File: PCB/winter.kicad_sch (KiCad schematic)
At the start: 131 parts, among them SW1 SW_Push, SW10 SW_Push, SW11 SW_Push, SW12 SW_Push, SW13 SW_Push, SW14 SW_Push, SW15 SW_Push, SW16 SW_Push, SW17 SW_Push, SW18 SW_Push, SW19 SW_Push, SW2 SW_Push, SW20 SW_Push, SW21 SW_Push, SW22 SW_Push, SW23 SW_Push, SW24 SW_Push, SW25 SW_Push, SW26 SW_Push, SW27 SW_Push, SW28 SW_Push, SW29 SW_Push, SW3 SW_Push, SW30 SW_Push, SW31 SW_Push, SW32 SW_Push, SW33 SW_Push, SW34 SW_Push, SW35 SW_Push, SW36 SW_Push, SW37 SW_Push, SW38 SW_Push, SW39 SW_Push, SW4 SW_Push, SW40 SW_Push, SW41 SW_Push, SW42 SW_Push, SW43 SW_Push, SW44 SW_Push, SW45 SW_Push, SW46 SW_Push, SW47 SW_Push, SW48 SW_Push, SW49 SW_Push, SW5 SW_Push, SW50 SW_Push, SW51 SW_Push, SW52 SW_Push, SW53 SW_Push, SW54 SW_Push, SW55 SW_Push, SW56 SW_Push, SW57 SW_Push, SW58 SW_Push, SW59 SW_Push, SW6 SW_Push, SW60 SW_Push, SW61 SW_Push, SW62 SW_Push, SW63 SW_Push, SW64 SW_Push, SW65 SW_Push, SW7 SW_Push, SW8 SW_Push, SW9 SW_Push, U1 RP2040-ZERO

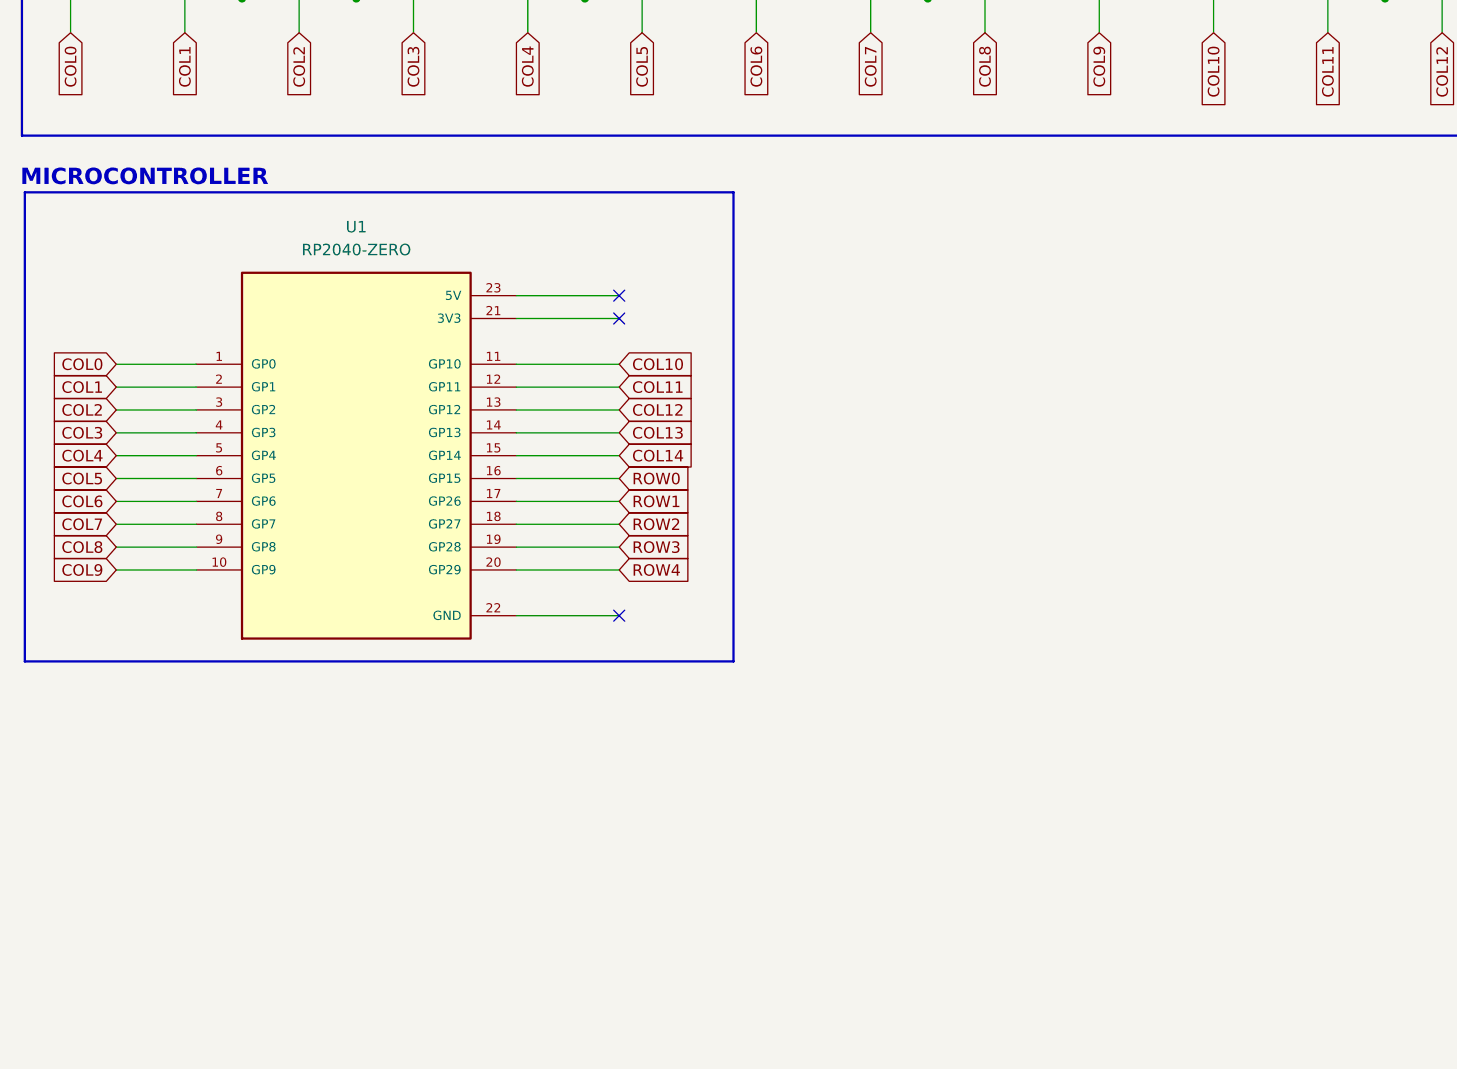
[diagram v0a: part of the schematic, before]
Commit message: changed mcu and added screen and knob
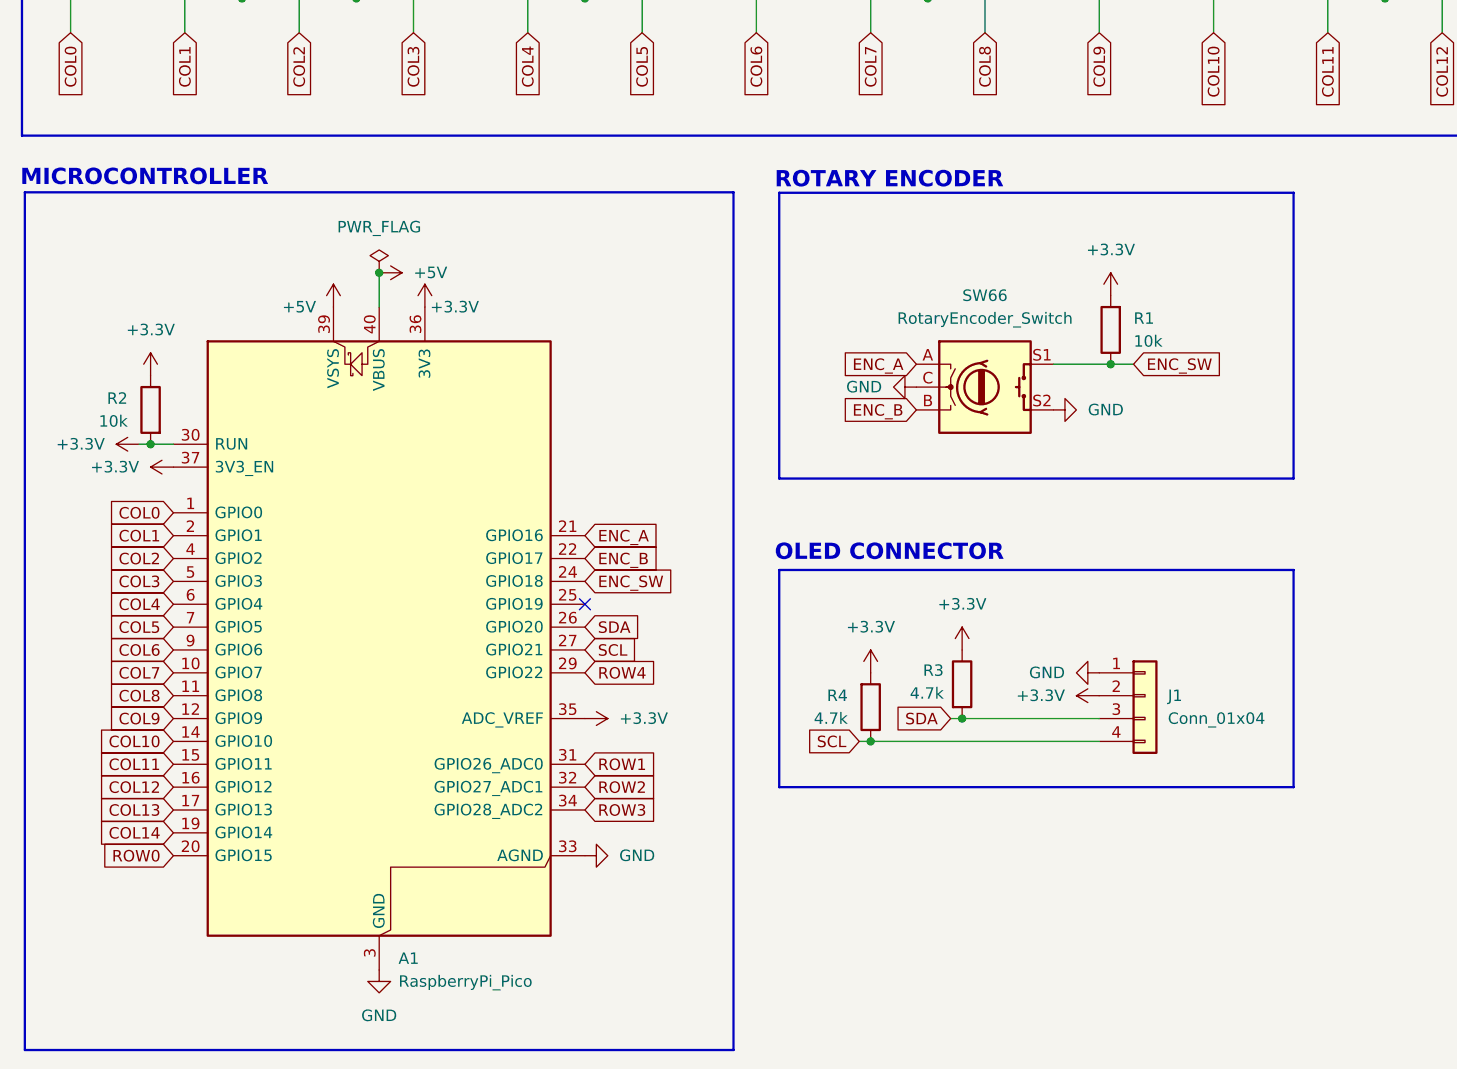
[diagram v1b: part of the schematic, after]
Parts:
- removed U1: RP2040-ZERO, RP2040-ZERO:MODULE_RP2040-ZERO, symbol RP2040-ZERO:RP2040-ZERO
- added A1: RaspberryPi_Pico, Module:RaspberryPi_Pico_Common_Unspecified, symbol MCU_Module:RaspberryPi_Pico
- added J1: Conn_01x04, Connector_PinHeader_2.54mm:PinHeader_1x04_P2.54mm_Vertical, symbol Connector_Generic:Conn_01x04
- added R1, R2: 10k, Resistor_SMD:R_0805_2012Metric, symbol Device:R
- added R3, R4: 4.7k, Resistor_SMD:R_0805_2012Metric, symbol Device:R
- added SW66: RotaryEncoder_Switch, Rotary_Encoder:RotaryEncoder_Alps_EC11E-Switch_Vertical_H20mm, symbol Device:RotaryEncoder_Switch
- SW1, SW10, SW11, SW12, SW13, SW15, SW17, SW18, SW19, SW2, SW20, SW21, SW22, SW23, SW24, SW25, SW26, SW27, SW28, SW3, SW30, SW32, SW33, SW34, SW35, SW36, SW37, SW38, SW39, SW4, SW40, SW41, SW42, SW44, SW46, SW47, SW48, SW49, SW5, SW50, SW51, SW52, SW53, SW54, SW55, SW57, SW6, SW7, SW8, SW9: footprint Switch_Keyboard_Hotswap_Kailh:SW_Hotswap_Kailh_MX_1.00u -> MX_Hotswap:MX-Hotswap-1U
- SW14: footprint Switch_Keyboard_Hotswap_Kailh:SW_Hotswap_Kailh_MX_2.00u -> MX_Hotswap:MX-Hotswap-1U
- SW16, SW29: footprint Switch_Keyboard_Hotswap_Kailh:SW_Hotswap_Kailh_MX_1.50u -> MX_Hotswap:MX-Hotswap-1U
- SW31: footprint Switch_Keyboard_Hotswap_Kailh:SW_Hotswap_Kailh_MX_1.75u -> MX_Hotswap:MX-Hotswap-1U
- SW43, SW45: footprint Switch_Keyboard_Hotswap_Kailh:SW_Hotswap_Kailh_MX_2.25u -> MX_Hotswap:MX-Hotswap-1U
- SW56: footprint Switch_Keyboard_Hotswap_Kailh:SW_Hotswap_Kailh_MX_2.75u -> MX_Hotswap:MX-Hotswap-1U
- SW58, SW59, SW60, SW62, SW63, SW64, SW65: footprint Switch_Keyboard_Hotswap_Kailh:SW_Hotswap_Kailh_MX_1.25u -> MX_Hotswap:MX-Hotswap-1U
- SW61: footprint Switch_Keyboard_Hotswap_Kailh:SW_Hotswap_Kailh_MX_6.25u -> MX_Hotswap:MX-Hotswap-1U
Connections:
- net COL0: now also A1.1 (GPIO0)
- net COL1: now also A1.2 (GPIO1)
- net COL10: now also A1.14 (GPIO10)
- net COL11: now also A1.15 (GPIO11)
- net COL12: now also A1.16 (GPIO12)
- net COL13: now also A1.17 (GPIO13)
- net COL14: now also A1.19 (GPIO14)
- net COL2: now also A1.4 (GPIO2)
- net COL3: now also A1.5 (GPIO3)
- net COL4: now also A1.6 (GPIO4)
- net COL5: now also A1.7 (GPIO5)
- net COL6: now also A1.9 (GPIO6)
- net COL7: now also A1.10 (GPIO7)
- net COL8: now also A1.11 (GPIO8)
- net COL9: now also A1.12 (GPIO9)
- net ROW0: now also A1.20 (GPIO15)
- net ROW1: now also A1.31 (GPIO26_ADC0)
- net ROW2: now also A1.32 (GPIO27_ADC1)
- net ROW3: now also A1.34 (GPIO28_ADC2)
- net ROW4: now also A1.29 (GPIO22)
- new net +3.3V: A1.30 (RUN), A1.35 (ADC_VREF), A1.36 (3V3), A1.37 (3V3_EN), J1.2 (Pin_2), R1.2, R2.1, R2.2, R3.1, R4.2
- new net +5V: A1.39 (VSYS), A1.40 (VBUS)
- new net ENC_A: A1.21 (GPIO16), SW66.A
- new net ENC_B: A1.22 (GPIO17), SW66.B
- new net ENC_SW: A1.24 (GPIO18), R1.1, SW66.S1
- new net GND: A1.13 (GND), A1.18 (GND), A1.23 (GND), A1.28 (GND), A1.3 (GND), A1.33 (AGND), A1.38 (GND), A1.8 (GND), J1.1 (Pin_1), SW66.C, SW66.S2
- new net SCL: A1.27 (GPIO21), J1.4 (Pin_4), R4.1
- new net SDA: A1.26 (GPIO20), J1.3 (Pin_3), R3.2
- no-connect marks 3 -> 1
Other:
- note added: "OLED CONNECTOR"
- note added: "ROTARY ENCODER"
